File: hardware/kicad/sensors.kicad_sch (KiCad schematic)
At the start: 29 parts, among them J3 JST SM06B-GHS-TB (SEN66-SIN-T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, J4 1x5 P1.27mm through-hole head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, J7 1x8 P2.54 mm female socket (M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, J8 1x8 P2.54 mm female socket (M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

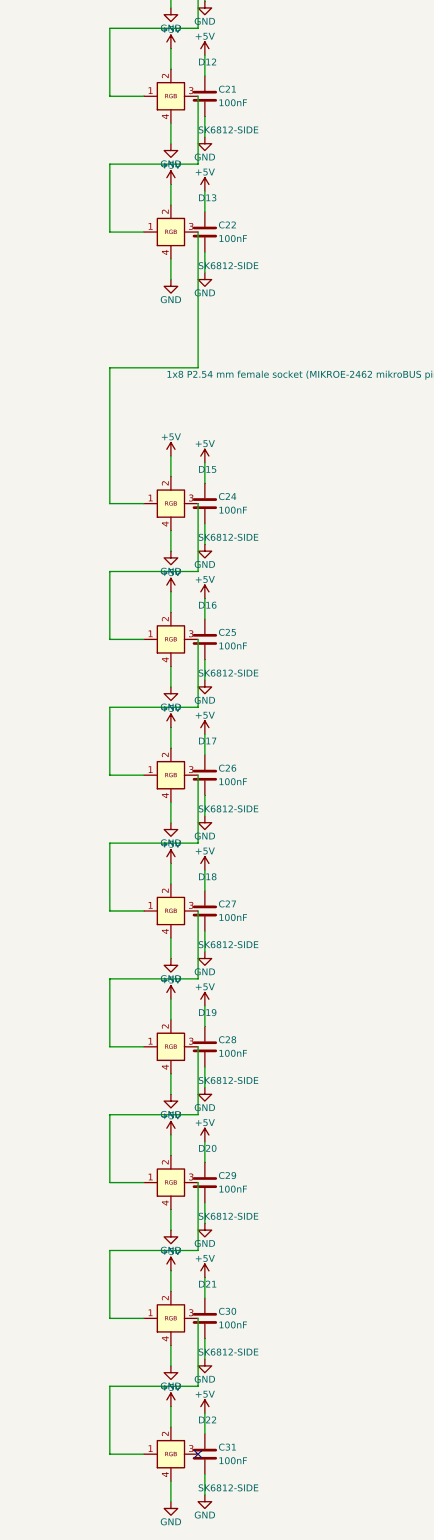
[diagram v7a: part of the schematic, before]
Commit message: feat(led-ring): shrink AQI ring to 8 slots @ 45 deg pitch (7 placed, D13 skipped)
LED ring redesign for cheaper SMT assembly: standard-multiple (45 deg)
placement angles instead of 30 deg avoids JLCPCB per-part rotation
overhead for non-standard angles. 8 ring slots * (270 - theta) deg
KiCad rotation, with index 2 skipped (D13 at theta=90 deg, blocked by
the J1 24 V terminal block courtyard south of the cable hole).

Final ring: 7 LEDs (D11, D12, D14..D18) + 7 caps (C20, C21, C23..C27),
all at standard 0/45/90/135 deg placement angles after the +180 deg
SK6812-SIDE pos.csv compensation. Chord between adjacent LEDs at R=13
becomes 9.95 mm (was 6.73 mm), giving 2.98 mm gap per side of the
4 mm LED body (was 1.37 mm).

JLCPCB_ROTATIONS_OAS cleanup (audit-19):
- SK6812-SIDE +180 entry KEPT. Empirically validated -- without it
  JLCPCB DFM renders the LEDs emitting inward, indicating JLCPCB
  tape-feeder reference is 180 deg offset from KiCad's footprint
  reference. Without the compensation, chip pin 1 (DIN) would land
  on PCB pad 4 (GND trace) -> reverse-polarity destruction.
- TO-263 (U1) and SOT-583 (U2) entries REMOVED. Those were empirical
  without DFM re-upload validation. Stock KiCad footprint pad geometry
  is verbatim correct (audit-15/16); without confirmed JLCPCB
  tape-feeder offset for these packages, compensation should not be
  applied speculatively. Re-add only if a future DFM upload shows
  U1/U2 mis-oriented.

ROUTING_CHUNKS temporarily reduced to ("gnd",) only -- the autoroute
snapshot in oas_routes.py and hand_v40 hand-route stubs both reference
segment endpoints at the OLD 12-LED positions which no longer exist.
Restore the full tuple after running Freerouting externally on the
new 8-LED layout and re-running tools/extract_routes.py.

Verification:
- 20/20 pipeline stages PASS in 109.3 s
- 17 .kicad_* files bit-identical across two consecutive runs
- DRC: 0 violations + 89 WARN-level unconnected pads (signal nets;
  GND copper pour reconnects ever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
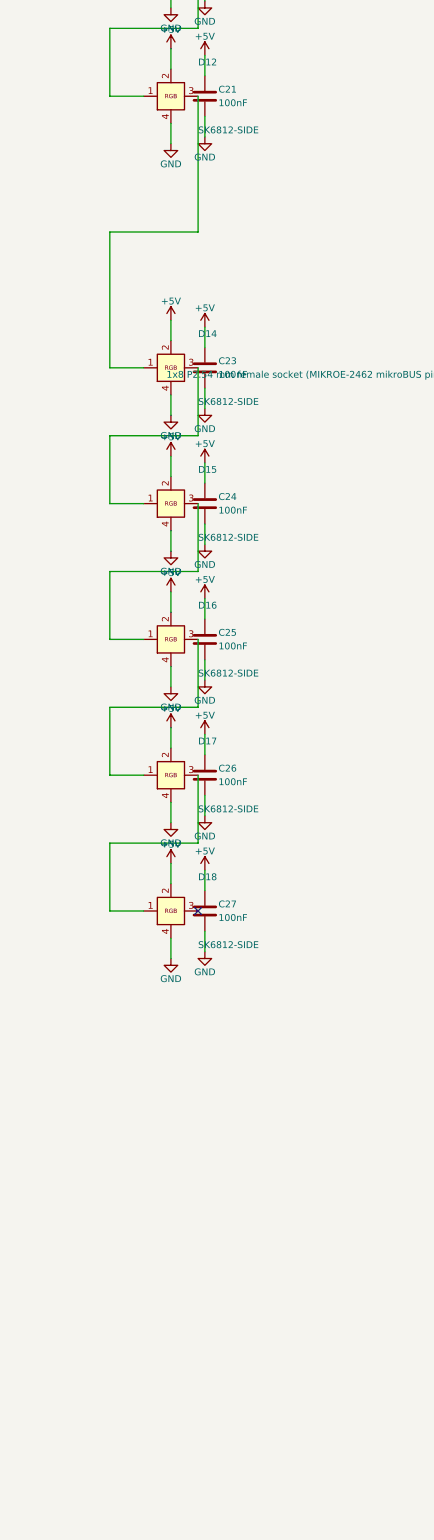
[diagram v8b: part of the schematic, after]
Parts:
- removed C22, C28, C29, C30, C31: 100nF, Capacitor_SMD:C_0402_1005Metric, symbol Device:C
- removed D13, D19, D20, D21, D22: SK6812-SIDE, oas:SK6812-SIDE, symbol OAS:SK6812-SIDE
- added C23: 100nF, Capacitor_SMD:C_0402_1005Metric, symbol Device:C
- added D14: SK6812-SIDE, oas:SK6812-SIDE, symbol OAS:SK6812-SIDE
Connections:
- net +5V: now also C23.1, D14.2 (VDD)
- net GND: now also C23.2, D14.4 (GND)
- net at D12.3 (DOUT): now also D14.1 (DIN)
- net at D15.1 (DIN): now also D14.3 (DOUT)
